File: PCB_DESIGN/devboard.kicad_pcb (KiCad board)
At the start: 2 copper layers, 21 x 51 mm, 33 parts, among them J1 USB_C_Receptacle_USB2.0_14P, J2 Conn_01x20, J3 Conn_01x20, J4 Conn_01x03, SW1 SW_Push, U1 RP2040, U2 MCP1700x-330xxTT, U4 W25Q16JVUXIQ TR, Y1 12 MHz

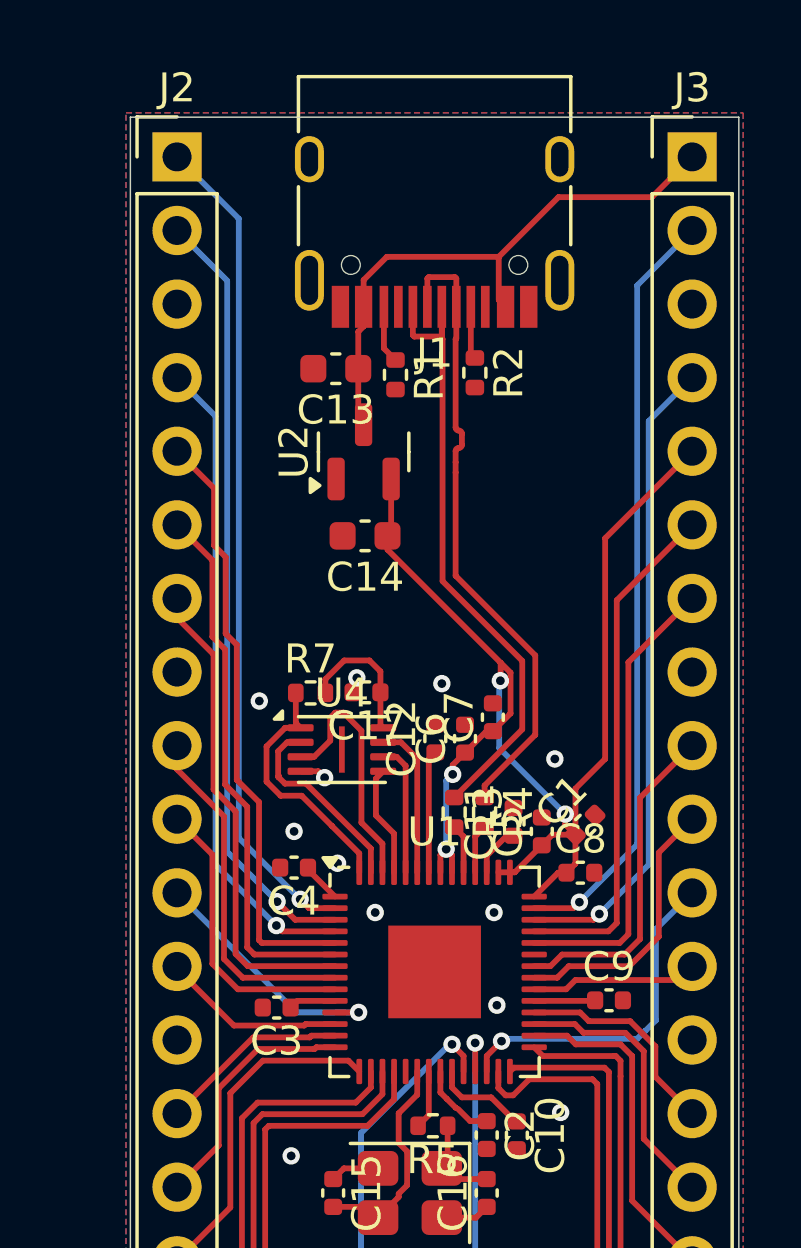
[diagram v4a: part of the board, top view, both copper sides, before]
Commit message: all the GND's and thermal relief stuff
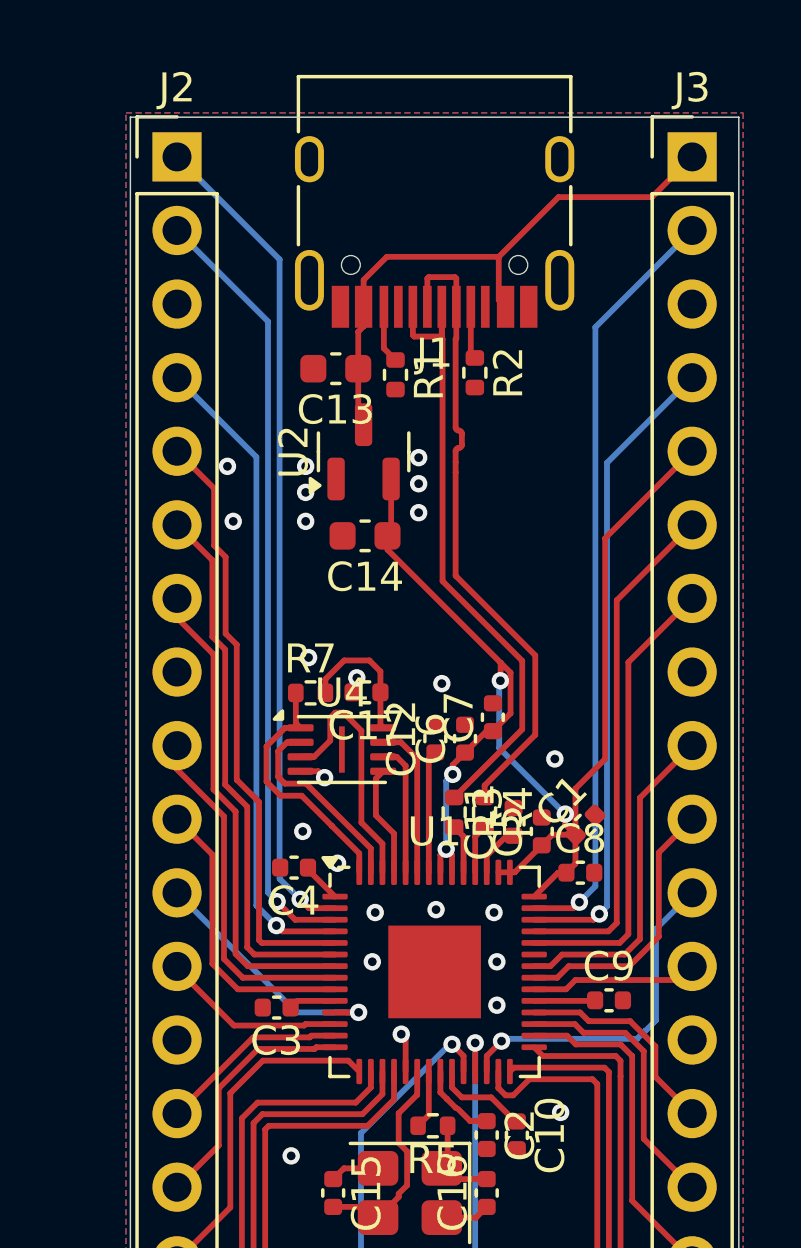
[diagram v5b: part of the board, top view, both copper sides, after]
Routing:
- net GND: track 4.89 -> 6.24 mm, vias 12 -> 24
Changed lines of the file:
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@@
+	)
+	(segment
+		(start 159.65 79.6875)
+		(end 159.65 78.55)
+		(width 0.2)
+		(layer "F.Cu")
+		(net 1)
 	)
 	(segment
@@
 	)
 	(segment
+		(start 159.65 78.55)
+		(end 159.5 78.4)
+		(width 0.2)
+		(layer "F.Cu")
+		(net 1)
+	)
+	(segment
 		(start 157.82 66.6)
 		(end 157.82 66.245446)
@@
 	)
 	(via
+		(at 153.5 58.8)
+		(size 0.6)
+		(drill 0.3)
+		(layers "F.Cu" "B.Cu")
+		(free yes)
+		(net 1)
+	)
+	(via
 		(at 162.8 77.4)
 		(size 0.6)
@@
 	)
 	(via
+		(at 160.7 74.1)
+		(size 0.6)
+		(drill 0.3)
+		(layers "F.Cu" "B.Cu")
+		(free yes)
+		(net 1)
+	)
+	(via
 		(at 157.3 72.5)
 		(size 0.6)
@@
 	)
 	(via
+		(at 162.8 75.9)
+		(size 0.6)
+		(drill 0.3)
+		(layers "F.Cu" "B.Cu")
+		(free yes)
+		(net 1)
+	)
+	(via
 		(at 160.9 66.3)
 		(size 0.6)
@@
 	)
 	(via
+		(at 156.1 71.4)
+		(size 0.6)
+		(drill 0.3)
+		(layers "F.Cu" "B.Cu")
+		(free yes)
+		(net 1)
+	)
+	(via
 		(at 165 81.1)
 		(size 0.6)
@@
 	)
 	(via
+		(at 156.2 60.7)
+		(size 0.6)
+		(drill 0.3)
+		(layers "F.Cu" "B.Cu")
+		(free yes)
+		(net 1)
+	)
+	(via
+		(at 153.7 60.7)
+		(size 0.6)
+		(drill 0.3)
+		(layers "F.Cu" "B.Cu")
+		(free yes)
+		(net 1)
+	)
+	(via
 		(at 158.6 74.2)
 		(size 0.6)
@@
 	)
 	(via
+		(at 160.1 58.5)
+		(size 0.6)
+		(drill 0.3)
+		(layers "F.Cu" "B.Cu")
+		(free yes)
+		(net 1)
+	)
+	(via
 		(at 155.7 82.6)
 		(size 0.6)
@@
 	)
 	(via
+		(at 158.5 75.9)
+		(size 0.6)
+		(drill 0.3)
+		(layers "F.Cu" "B.Cu")
+		(free yes)
+		(net 1)
+	)
+	(via
 		(at 157.965446 66.1)
 		(size 0.6)
@@
 	)
 	(via
-		(at 155.8 71.4)
-		(size 0.6)
-		(drill 0.3)
-		(layers "F.Cu" "B.Cu")
-		(free yes)
-		(net 1)
-	)
-	(via
-		(at 154.6 66.9)
+		(at 160.1 60.4)
+		(size 0.6)
+		(drill 0.3)
+		(layers "F.Cu" "B.Cu")
+		(free yes)
+		(net 1)
+	)
+	(via
+		(at 156.2 58.8)
+		(size 0.6)
+		(drill 0.3)
+		(layers "F.Cu" "B.Cu")
+		(free yes)
+		(net 1)
+	)
+	(via
+		(at 159.5 78.4)
+		(size 0.6)
+		(drill 0.3)
+		(layers "F.Cu" "B.Cu")
+		(free yes)
+		(net 1)
+	)
+	(via
+		(at 156.3 65.4)
+		(size 0.6)
+		(drill 0.3)
+		(layers "F.Cu" "B.Cu")
+		(free yes)
+		(net 1)
+	)
+	(via
+		(at 156.2 59.7)
+		(size 0.6)
+		(drill 0.3)
+		(layers "F.Cu" "B.Cu")
+		(free yes)
+		(net 1)
+	)
+	(via
+		(at 160.1 59.4)
 		(size 0.6)
 		(drill 0.3)
@@
 	)
 	(segment
-		(start 153.491 52.391)
+		(start 154.9 73.511471)
+		(end 154.9 53.8)
+		(width 0.2)
+		(layer "B.Cu")
+		(net 13)
+	)
+	(segment
+		(start 155.214263 73.825734)
+		(end 154.9 73.511471)
+		(width 0.2)
+		(layer "B.Cu")
+		(net 13)
+	)
+	(segment
+		(start 154.9 53.8)
 		(end 151.76 50.66)
-		(width 0.2)
-		(layer "B.Cu")
-		(net 13)
-	)
-	(segment
-		(start 155.214263 73.825734)
-		(end 153.491 72.102471)
-		(width 0.2)
-		(layer "B.Cu")
-		(net 13)
-	)
-	(segment
-		(start 153.491 72.102471)
-		(end 153.491 52.391)
 		(width 0.2)
 		(layer "B.Cu")
@@
 	)
 	(segment
+		(start 155.301 51.661)
+		(end 151.76 48.12)
+		(width 0.2)
+		(layer "B.Cu")
+		(net 17)
+	)
+	(segment
 		(start 156.010053 73.743738)
-		(end 153.892 71.625685)
+		(end 155.301 73.034685)
 		(width 0.2)
 		(layer "B.Cu")
@@
 	)
 	(segment
-		(start 153.892 71.625685)
-		(end 153.892 50.252)
-		(width 0.2)
-		(layer "B.Cu")
-		(net 17)
-	)
-	(segment
-		(start 153.892 50.252)
-		(end 151.76 48.12)
+		(start 155.301 73.034685)
+		(end 155.301 51.661)
 		(width 0.2)
 		(layer "B.Cu")
@@
 	)
 	(segment
-		(start 153.09 72.55)
-		(end 153.09 57.07)
+		(start 154.499 73.959)
+		(end 154.499 58.479)
 		(width 0.2)
 		(layer "B.Cu")
@@
 	)
 	(segment
+		(start 154.499 58.479)
+		(end 151.76 55.74)
+		(width 0.2)
+		(layer "B.Cu")
+		(net 19)
+	)
+	(segment
 		(start 155.19 74.65)
-		(end 153.09 72.55)
-		(width 0.2)
-		(layer "B.Cu")
-		(net 19)
-	)
-	(segment
-		(start 153.09 57.07)
-		(end 151.76 55.74)
+		(end 154.499 73.959)
 		(width 0.2)
 		(layer "B.Cu")
@@
 	(segment
 		(start 165.648236 73.843049)
-		(end 167.64 71.851285)
+		(end 166.2 73.291285)
 		(width 0.2)
 		(layer "B.Cu")
@@
 	)
 	(segment
-		(start 167.64 52.56)
+		(start 166.2 73.291285)
+		(end 166.2 54)
+		(width 0.2)
+		(layer "B.Cu")
+		(net 25)
+	)
+	(segment
+		(start 166.2 54)
 		(end 169.54 50.66)
-		(width 0.2)
-		(layer "B.Cu")
-		(net 25)
-	)
-	(segment
-		(start 167.64 71.851285)
-		(end 167.64 52.56)
 		(width 0.2)
 		(layer "B.Cu")
@@
 	)
 	(segment
-		(start 168.04 57.24)
+		(start 166.337 74.25)
+		(end 166.6 73.987)
+		(width 0.2)
+		(layer "B.Cu")
+		(net 29)
+	)
+	(segment
+		(start 166.6 73.987)
+		(end 166.6 58.68)
+		(width 0.2)
+		(layer "B.Cu")
+		(net 29)
+	)
+	(segment
+		(start 166.6 58.68)
 		(end 169.54 55.74)
 		(width 0.2)
 		(layer "B.Cu")
-		(net 29)
-	)
-	(segment
-		(start 168.04 72.547)
-		(end 168.04 57.24)
-		(width 0.2)
-		(layer "B.Cu")
-		(net 29)
-	)
-	(segment
-		(start 166.337 74.25)
-		(end 168.04 72.547)
-		(width 0.2)
-		(layer "B.Cu")

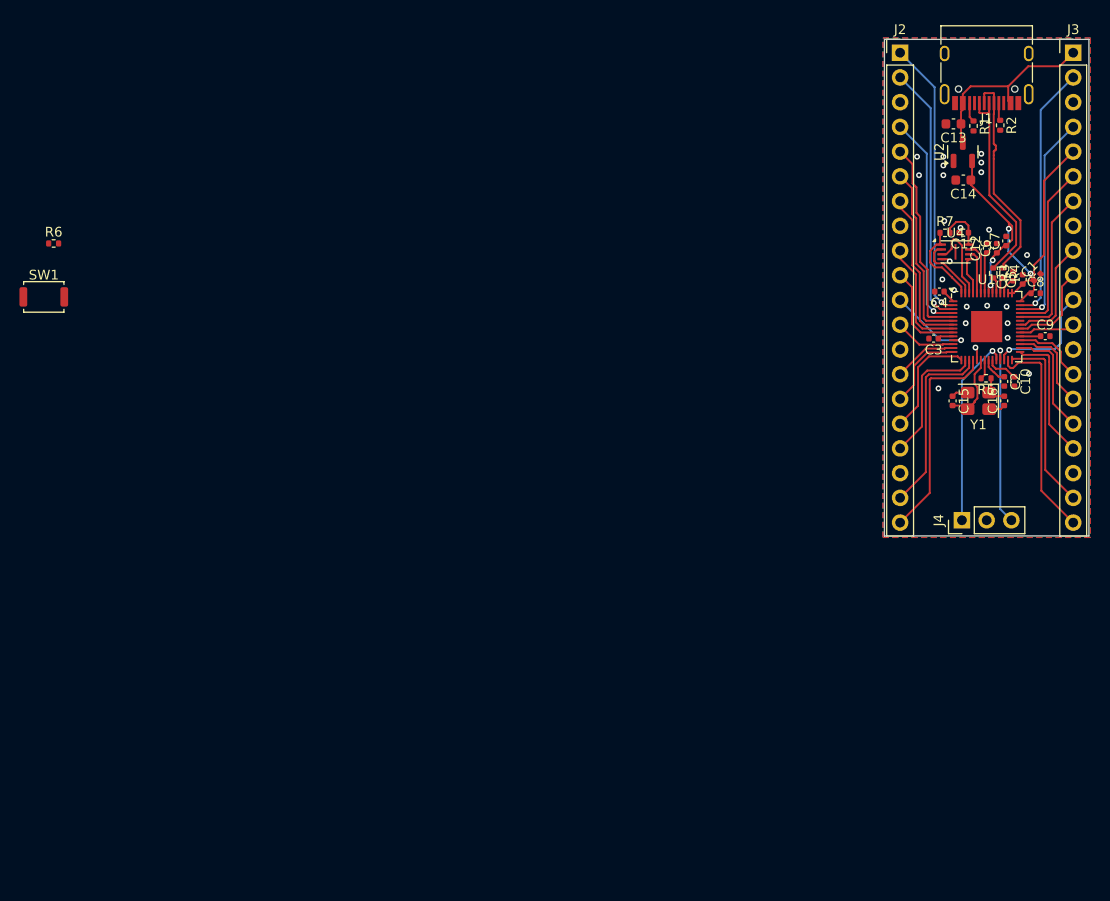
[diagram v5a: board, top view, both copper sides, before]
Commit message: removed all ratlines
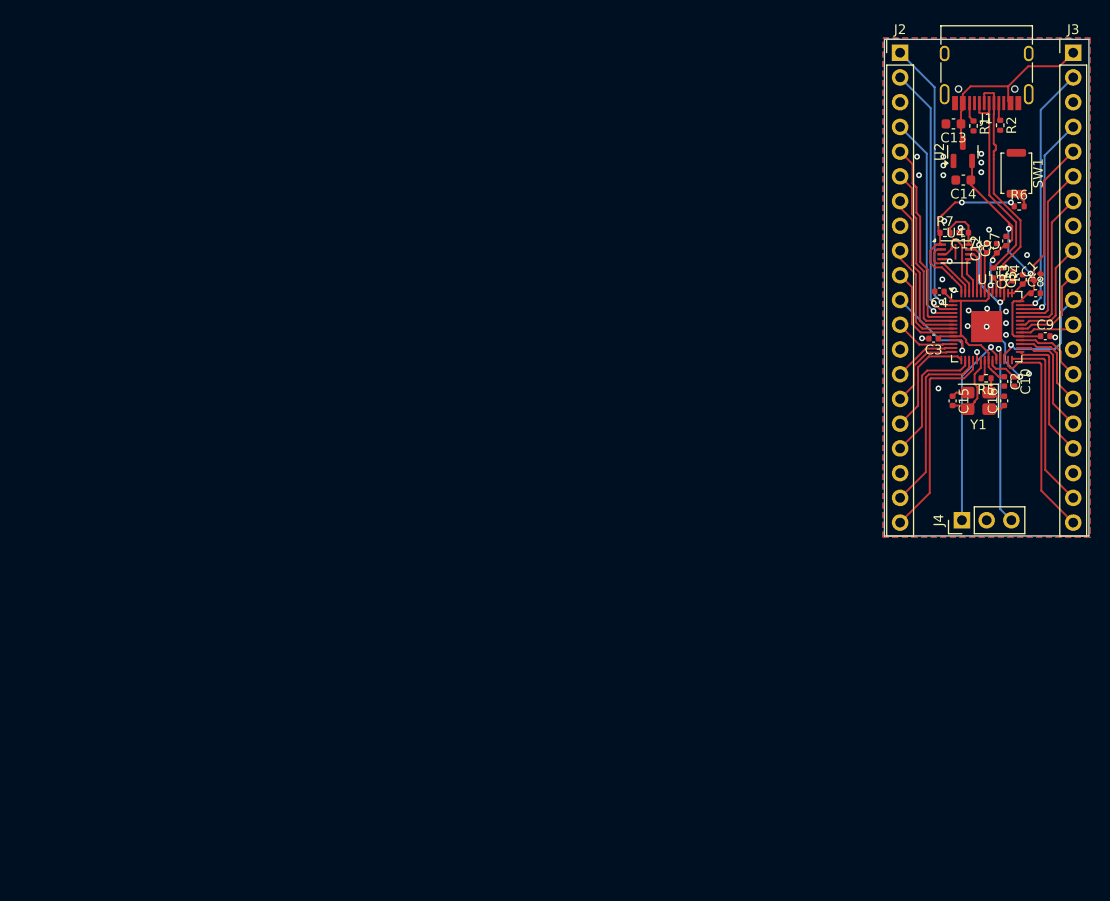
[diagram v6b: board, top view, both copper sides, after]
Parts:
- moved SW1 100.7 mm to (163.7, 60.5), turned to -90 degrees
- moved R6 99.2 mm to (164.0, 63.9)
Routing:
- net +1V1: track 9.29 -> 30.9 mm, vias 0 -> 3
- net +3V3: track 57.9 -> 76.1 mm
- net QSPI_SS: track 8.81 -> 19.0 mm, vias 0 -> 2
- net GPIO8: track 8.79 -> 10.9 mm
- net Net-(R6-Pad2): track 0.00 -> 1.63 mm
- net GND: track 6.24 -> 7.03 mm, vias 24 -> 27
- net SWCLK: track 19.8 -> 20.6 mm
- net RUN: track 11.8 -> 12.3 mm

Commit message: fixing DRC
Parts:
- moved C1 36.1 mm to (158.6, 106.5)
- moved C11 36.1 mm to (156.1, 106.4)
- moved C12 36.1 mm to (153.4, 103.5)
- moved C15 36.1 mm to (149.9, 119.2)
- moved C16 36.1 mm to (155.2, 119.2)
- moved C17 36.1 mm to (151.0, 102.0)
- moved C2 36.1 mm to (155.2, 117.2)
- moved C7 36.1 mm to (155.4, 102.8)
- moved J4 36.1 mm to (150.8, 131.5)
- moved R3 36.1 mm to (154.1, 106.1)
- moved R4 36.1 mm to (155.1, 106.1)
- moved U2 36.1 mm to (150.9, 93.7)
- moved Y1 36.1 mm to (152.5, 119.2)
- moved C13 36.1 mm to (150.0, 90.8)
- moved J2 36.1 mm to (144.5, 83.5)
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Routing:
- net GND: track 7.03 -> 13.3 mm, vias 27 -> 30
- net +3V3: track 76.1 -> 80.9 mm
